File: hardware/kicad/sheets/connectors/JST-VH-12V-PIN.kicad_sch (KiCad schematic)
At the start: 5 parts, among them U58 VH3_96-2P_WZ

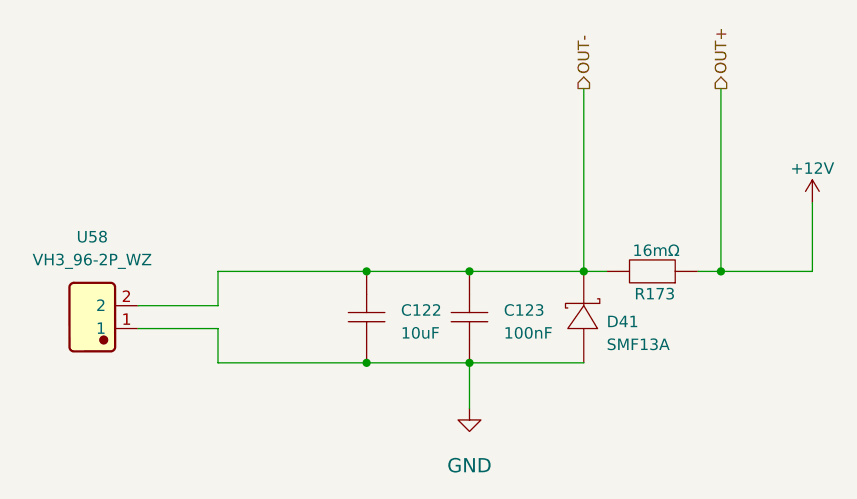
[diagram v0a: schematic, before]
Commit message: more sheet simplfiication and pre simpler 12v sym
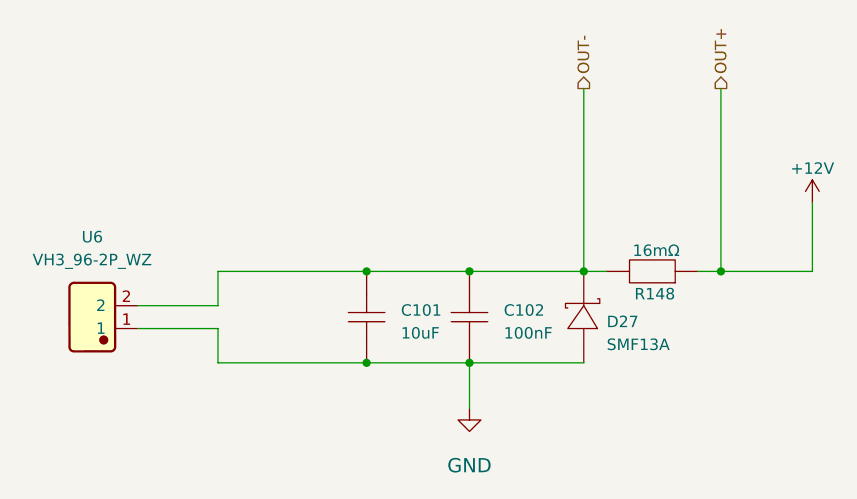
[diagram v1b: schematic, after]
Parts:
- renumbered C122 to C101, C123 to C102, D41 to D27, R173 to R148, U58 to U6

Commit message: resheeted bms and fixed links for the 12v buck
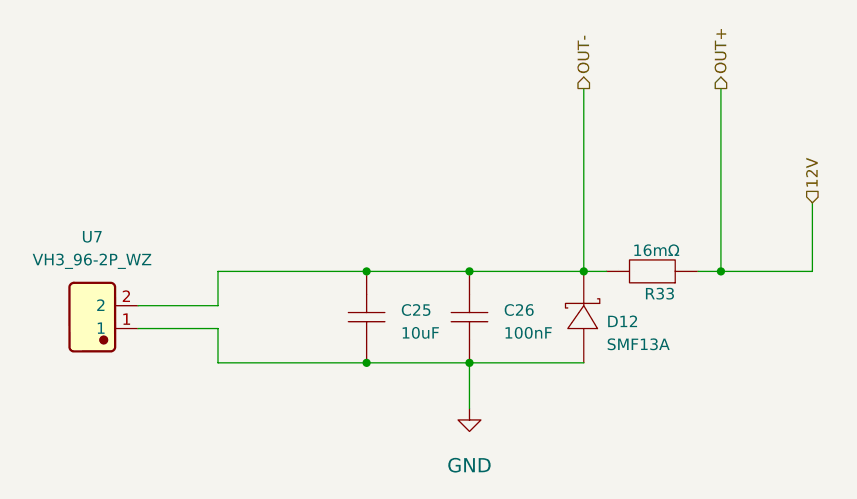
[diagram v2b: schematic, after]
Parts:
- renumbered C101 to C25, C102 to C26, D27 to D12, R148 to R33, U6 to U7
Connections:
- net +12V renamed 12V

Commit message: various improvements
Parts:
- renumbered C25 to C29, C26 to C30, D12 to D15, R33 to R35, U7 to U13
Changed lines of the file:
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@@
 		(on_board yes)
 		(dnp no)
-		(property "Reference" "U7"
+		(property "Reference" "U13"
 			(at 97.79 87.63 0)
 			(effects
@@
 			(project "svea_powerboard_rev3"
 				(path "/3f85abf4-0b95-4c4a-b7e9-06f59ca1ea3d/5c2e021f-c2d4-49e2-8c36-9a64f1f12001/03241f80-3125-4f5b-a1a0-add76ba31aaa"
-					(reference "U7")
-					(unit 1)
-				)
-				(path "/3f85abf4-0b95-4c4a-b7e9-06f59ca1ea3d/5c2e021f-c2d4-49e2-8c36-9a64f1f12001/b3c2b899-37d0-4be6-83c2-2e989d7fd2d2"
-					(reference "U8")
-					(unit 1)
-				)
-				(path "/3f85abf4-0b95-4c4a-b7e9-06f59ca1ea3d/5c2e021f-c2d4-49e2-8c36-9a64f1f12001/edc91f8c-d810-4cb3-9371-ed9a44c3aaeb"
-					(reference "U9")
+					(reference "U13")
+					(unit 1)
+				)
+				(path "/3f85abf4-0b95-4c4a-b7e9-06f59ca1ea3d/5c2e021f-c2d4-49e2-8c36-9a64f1f12001/782118f9-6c0b-4f5a-9c3b-1e5b8fc1f0ac"
+					(reference "U14")
+					(unit 1)
+				)
+				(path "/3f85abf4-0b95-4c4a-b7e9-06f59ca1ea3d/5c2e021f-c2d4-49e2-8c36-9a64f1f12001/beb9ceef-df3a-4e22-8974-012ce1407a41"
+					(reference "U15")
 					(unit 1)
 				)
@@
 		(on_board yes)
 		(dnp no)
-		(property "Reference" "D12"
+		(property "Reference" "D15"
 			(at 154.94 97.79 90)
 			(effects
@@
 			(project "svea_powerboard_rev3"
 				(path "/3f85abf4-0b95-4c4a-b7e9-06f59ca1ea3d/5c2e021f-c2d4-49e2-8c36-9a64f1f12001/03241f80-3125-4f5b-a1a0-add76ba31aaa"
-					(reference "D12")
-					(unit 1)
-				)
-				(path "/3f85abf4-0b95-4c4a-b7e9-06f59ca1ea3d/5c2e021f-c2d4-49e2-8c36-9a64f1f12001/b3c2b899-37d0-4be6-83c2-2e989d7fd2d2"
-					(reference "D13")
-					(unit 1)
-				)
-				(path "/3f85abf4-0b95-4c4a-b7e9-06f59ca1ea3d/5c2e021f-c2d4-49e2-8c36-9a64f1f12001/edc91f8c-d810-4cb3-9371-ed9a44c3aaeb"
-					(reference "D14")
+					(reference "D15")
+					(unit 1)
+				)
+				(path "/3f85abf4-0b95-4c4a-b7e9-06f59ca1ea3d/5c2e021f-c2d4-49e2-8c36-9a64f1f12001/782118f9-6c0b-4f5a-9c3b-1e5b8fc1f0ac"
+					(reference "D16")
+					(unit 1)
+				)
+				(path "/3f85abf4-0b95-4c4a-b7e9-06f59ca1ea3d/5c2e021f-c2d4-49e2-8c36-9a64f1f12001/beb9ceef-df3a-4e22-8974-012ce1407a41"
+					(reference "D17")
 					(unit 1)
 				)
@@
 		(on_board yes)
 		(dnp no)
-		(property "Reference" "C26"
+		(property "Reference" "C30"
 			(at 143.51 96.52 90)
 			(effects
@@
 			(project "svea_powerboard_rev3"
 				(path "/3f85abf4-0b95-4c4a-b7e9-06f59ca1ea3d/5c2e021f-c2d4-49e2-8c36-9a64f1f12001/03241f80-3125-4f5b-a1a0-add76ba31aaa"
-					(reference "C26")
-					(unit 1)
-				)
-				(path "/3f85abf4-0b95-4c4a-b7e9-06f59ca1ea3d/5c2e021f-c2d4-49e2-8c36-9a64f1f12001/b3c2b899-37d0-4be6-83c2-2e989d7fd2d2"
-					(reference "C28")
-					(unit 1)
-				)
-				(path "/3f85abf4-0b95-4c4a-b7e9-06f59ca1ea3d/5c2e021f-c2d4-49e2-8c36-9a64f1f12001/edc91f8c-d810-4cb3-9371-ed9a44c3aaeb"
 					(reference "C30")
+					(unit 1)
+				)
+				(path "/3f85abf4-0b95-4c4a-b7e9-06f59ca1ea3d/5c2e021f-c2d4-49e2-8c36-9a64f1f12001/782118f9-6c0b-4f5a-9c3b-1e5b8fc1f0ac"
+					(reference "C32")
+					(unit 1)
+				)
+				(path "/3f85abf4-0b95-4c4a-b7e9-06f59ca1ea3d/5c2e021f-c2d4-49e2-8c36-9a64f1f12001/beb9ceef-df3a-4e22-8974-012ce1407a41"
+					(reference "C34")
 					(unit 1)
 				)
@@
 		(on_board yes)
 		(dnp no)
-		(property "Reference" "#PWR035"
+		(property "Reference" "#PWR053"
 			(at 139.7 106.68 0)
 			(effects
@@
 			(project "svea_powerboard_rev3"
 				(path "/3f85abf4-0b95-4c4a-b7e9-06f59ca1ea3d/5c2e021f-c2d4-49e2-8c36-9a64f1f12001/03241f80-3125-4f5b-a1a0-add76ba31aaa"
-					(reference "#PWR035")
-					(unit 1)
-				)
-				(path "/3f85abf4-0b95-4c4a-b7e9-06f59ca1ea3d/5c2e021f-c2d4-49e2-8c36-9a64f1f12001/b3c2b899-37d0-4be6-83c2-2e989d7fd2d2"
-					(reference "#PWR036")
-					(unit 1)
-				)
-				(path "/3f85abf4-0b95-4c4a-b7e9-06f59ca1ea3d/5c2e021f-c2d4-49e2-8c36-9a64f1f12001/edc91f8c-d810-4cb3-9371-ed9a44c3aaeb"
-					(reference "#PWR037")
+					(reference "#PWR053")
+					(unit 1)
+				)
+				(path "/3f85abf4-0b95-4c4a-b7e9-06f59ca1ea3d/5c2e021f-c2d4-49e2-8c36-9a64f1f12001/782118f9-6c0b-4f5a-9c3b-1e5b8fc1f0ac"
+					(reference "#PWR054")
+					(unit 1)
+				)
+				(path "/3f85abf4-0b95-4c4a-b7e9-06f59ca1ea3d/5c2e021f-c2d4-49e2-8c36-9a64f1f12001/beb9ceef-df3a-4e22-8974-012ce1407a41"
+					(reference "#PWR055")
 					(unit 1)
 				)
@@
 		(on_board yes)
 		(dnp no)
-		(property "Reference" "C25"
+		(property "Reference" "C29"
 			(at 132.08 96.52 90)
 			(effects
@@
 			(project "svea_powerboard_rev3"
 				(path "/3f85abf4-0b95-4c4a-b7e9-06f59ca1ea3d/5c2e021f-c2d4-49e2-8c36-9a64f1f12001/03241f80-3125-4f5b-a1a0-add76ba31aaa"
-					(reference "C25")
-					(unit 1)
-				)
-				(path "/3f85abf4-0b95-4c4a-b7e9-06f59ca1ea3d/5c2e021f-c2d4-49e2-8c36-9a64f1f12001/b3c2b899-37d0-4be6-83c2-2e989d7fd2d2"
-					(reference "C27")
-					(unit 1)
-				)
-				(path "/3f85abf4-0b95-4c4a-b7e9-06f59ca1ea3d/5c2e021f-c2d4-49e2-8c36-9a64f1f12001/edc91f8c-d810-4cb3-9371-ed9a44c3aaeb"
 					(reference "C29")
+					(unit 1)
+				)
+				(path "/3f85abf4-0b95-4c4a-b7e9-06f59ca1ea3d/5c2e021f-c2d4-49e2-8c36-9a64f1f12001/782118f9-6c0b-4f5a-9c3b-1e5b8fc1f0ac"
+					(reference "C31")
+					(unit 1)
+				)
+				(path "/3f85abf4-0b95-4c4a-b7e9-06f59ca1ea3d/5c2e021f-c2d4-49e2-8c36-9a64f1f12001/beb9ceef-df3a-4e22-8974-012ce1407a41"
+					(reference "C33")
 					(unit 1)
 				)
@@
 		(on_board yes)
 		(dnp no)
-		(property "Reference" "R33"
+		(property "Reference" "R35"
 			(at 162.56 93.218 0)
 			(effects
@@
 			(project "svea_powerboard_rev3"
 				(path "/3f85abf4-0b95-4c4a-b7e9-06f59ca1ea3d/5c2e021f-c2d4-49e2-8c36-9a64f1f12001/03241f80-3125-4f5b-a1a0-add76ba31aaa"
-					(reference "R33")
-					(unit 1)
-				)
-				(path "/3f85abf4-0b95-4c4a-b7e9-06f59ca1ea3d/5c2e021f-c2d4-49e2-8c36-9a64f1f12001/b3c2b899-37d0-4be6-83c2-2e989d7fd2d2"
-					(reference "R34")
-					(unit 1)
-				)
-				(path "/3f85abf4-0b95-4c4a-b7e9-06f59ca1ea3d/5c2e021f-c2d4-49e2-8c36-9a64f1f12001/edc91f8c-d810-4cb3-9371-ed9a44c3aaeb"
 					(reference "R35")
 					(unit 1)
 				)
+				(path "/3f85abf4-0b95-4c4a-b7e9-06f59ca1ea3d/5c2e021f-c2d4-49e2-8c36-9a64f1f12001/782118f9-6c0b-4f5a-9c3b-1e5b8fc1f0ac"
+					(reference "R36")
+					(unit 1)
+				)
+				(path "/3f85abf4-0b95-4c4a-b7e9-06f59ca1ea3d/5c2e021f-c2d4-49e2-8c36-9a64f1f12001/beb9ceef-df3a-4e22-8974-012ce1407a41"
+					(reference "R37")
+					(unit 1)
+				)

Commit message: various improvements
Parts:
- renumbered C29 to C36, C30 to C37, D15 to D18, R35 to R44
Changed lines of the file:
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@@
 		(on_board yes)
 		(dnp no)
-		(property "Reference" "D15"
+		(property "Reference" "D18"
 			(at 154.94 97.79 90)
 			(effects
@@
 			(project "svea_powerboard_rev3"
 				(path "/3f85abf4-0b95-4c4a-b7e9-06f59ca1ea3d/5c2e021f-c2d4-49e2-8c36-9a64f1f12001/03241f80-3125-4f5b-a1a0-add76ba31aaa"
-					(reference "D15")
+					(reference "D18")
 					(unit 1)
 				)
 				(path "/3f85abf4-0b95-4c4a-b7e9-06f59ca1ea3d/5c2e021f-c2d4-49e2-8c36-9a64f1f12001/782118f9-6c0b-4f5a-9c3b-1e5b8fc1f0ac"
-					(reference "D16")
+					(reference "D19")
 					(unit 1)
 				)
 				(path "/3f85abf4-0b95-4c4a-b7e9-06f59ca1ea3d/5c2e021f-c2d4-49e2-8c36-9a64f1f12001/beb9ceef-df3a-4e22-8974-012ce1407a41"
-					(reference "D17")
+					(reference "D20")
 					(unit 1)
 				)
@@
 		(on_board yes)
 		(dnp no)
-		(property "Reference" "C30"
+		(property "Reference" "C37"
 			(at 143.51 96.52 90)
 			(effects
@@
 			(project "svea_powerboard_rev3"
 				(path "/3f85abf4-0b95-4c4a-b7e9-06f59ca1ea3d/5c2e021f-c2d4-49e2-8c36-9a64f1f12001/03241f80-3125-4f5b-a1a0-add76ba31aaa"
-					(reference "C30")
+					(reference "C37")
 					(unit 1)
 				)
 				(path "/3f85abf4-0b95-4c4a-b7e9-06f59ca1ea3d/5c2e021f-c2d4-49e2-8c36-9a64f1f12001/782118f9-6c0b-4f5a-9c3b-1e5b8fc1f0ac"
-					(reference "C32")
+					(reference "C39")
 					(unit 1)
 				)
 				(path "/3f85abf4-0b95-4c4a-b7e9-06f59ca1ea3d/5c2e021f-c2d4-49e2-8c36-9a64f1f12001/beb9ceef-df3a-4e22-8974-012ce1407a41"
-					(reference "C34")
+					(reference "C41")
 					(unit 1)
 				)
@@
 		(on_board yes)
 		(dnp no)
-		(property "Reference" "#PWR053"
+		(property "Reference" "#PWR061"
 			(at 139.7 106.68 0)
 			(effects
@@
 			(project "svea_powerboard_rev3"
 				(path "/3f85abf4-0b95-4c4a-b7e9-06f59ca1ea3d/5c2e021f-c2d4-49e2-8c36-9a64f1f12001/03241f80-3125-4f5b-a1a0-add76ba31aaa"
-					(reference "#PWR053")
+					(reference "#PWR061")
 					(unit 1)
 				)
 				(path "/3f85abf4-0b95-4c4a-b7e9-06f59ca1ea3d/5c2e021f-c2d4-49e2-8c36-9a64f1f12001/782118f9-6c0b-4f5a-9c3b-1e5b8fc1f0ac"
-					(reference "#PWR054")
+					(reference "#PWR062")
 					(unit 1)
 				)
 				(path "/3f85abf4-0b95-4c4a-b7e9-06f59ca1ea3d/5c2e021f-c2d4-49e2-8c36-9a64f1f12001/beb9ceef-df3a-4e22-8974-012ce1407a41"
-					(reference "#PWR055")
+					(reference "#PWR063")
 					(unit 1)
 				)
@@
 		(on_board yes)
 		(dnp no)
-		(property "Reference" "C29"
+		(property "Reference" "C36"
 			(at 132.08 96.52 90)
 			(effects
@@
 			(project "svea_powerboard_rev3"
 				(path "/3f85abf4-0b95-4c4a-b7e9-06f59ca1ea3d/5c2e021f-c2d4-49e2-8c36-9a64f1f12001/03241f80-3125-4f5b-a1a0-add76ba31aaa"
-					(reference "C29")
+					(reference "C36")
 					(unit 1)
 				)
 				(path "/3f85abf4-0b95-4c4a-b7e9-06f59ca1ea3d/5c2e021f-c2d4-49e2-8c36-9a64f1f12001/782118f9-6c0b-4f5a-9c3b-1e5b8fc1f0ac"
-					(reference "C31")
+					(reference "C38")
 					(unit 1)
 				)
 				(path "/3f85abf4-0b95-4c4a-b7e9-06f59ca1ea3d/5c2e021f-c2d4-49e2-8c36-9a64f1f12001/beb9ceef-df3a-4e22-8974-012ce1407a41"
-					(reference "C33")
+					(reference "C40")
 					(unit 1)
 				)
@@
 		(on_board yes)
 		(dnp no)
-		(property "Reference" "R35"
+		(property "Reference" "R44"
 			(at 162.56 93.218 0)
 			(effects
@@
 			(project "svea_powerboard_rev3"
 				(path "/3f85abf4-0b95-4c4a-b7e9-06f59ca1ea3d/5c2e021f-c2d4-49e2-8c36-9a64f1f12001/03241f80-3125-4f5b-a1a0-add76ba31aaa"
-					(reference "R35")
+					(reference "R44")
 					(unit 1)
 				)
 				(path "/3f85abf4-0b95-4c4a-b7e9-06f59ca1ea3d/5c2e021f-c2d4-49e2-8c36-9a64f1f12001/782118f9-6c0b-4f5a-9c3b-1e5b8fc1f0ac"
-					(reference "R36")
+					(reference "R45")
 					(unit 1)
 				)
 				(path "/3f85abf4-0b95-4c4a-b7e9-06f59ca1ea3d/5c2e021f-c2d4-49e2-8c36-9a64f1f12001/beb9ceef-df3a-4e22-8974-012ce1407a41"
-					(reference "R37")
-					(unit 1)
-				)
+					(reference "R46")
+					(unit 1)
+				)

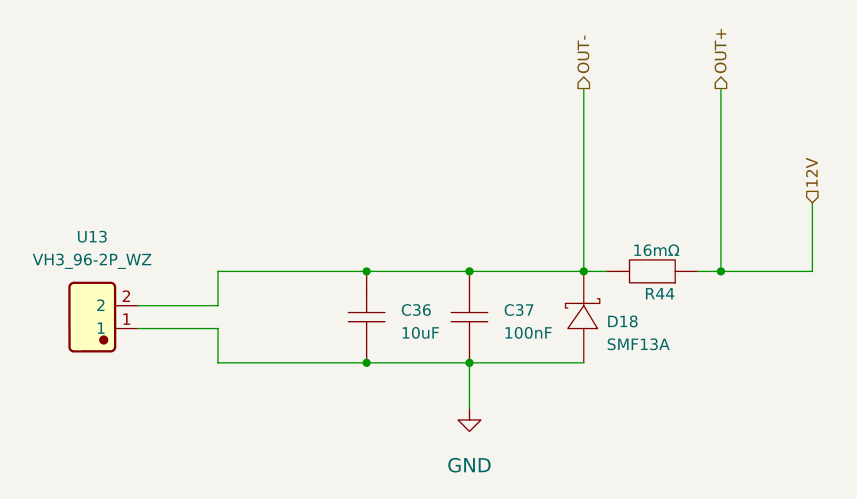
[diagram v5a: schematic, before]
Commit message: current sensing on the servos and cleaning up empty sheets
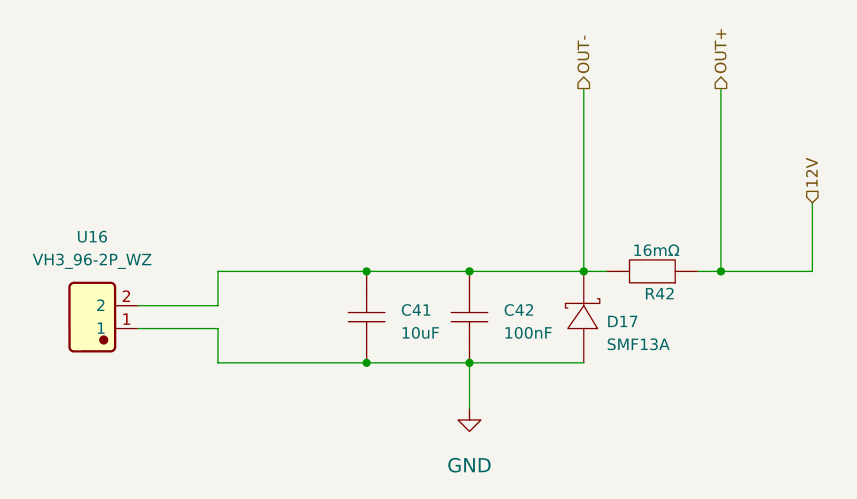
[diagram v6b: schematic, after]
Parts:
- renumbered C36 to C41, C37 to C42, D18 to D17, R44 to R42, U13 to U16
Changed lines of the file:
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@@
 		(on_board yes)
 		(dnp no)
-		(property "Reference" "U13"
+		(property "Reference" "U16"
 			(at 97.79 87.63 0)
 			(effects
@@
 			(project "svea_powerboard_rev3"
 				(path "/3f85abf4-0b95-4c4a-b7e9-06f59ca1ea3d/5c2e021f-c2d4-49e2-8c36-9a64f1f12001/03241f80-3125-4f5b-a1a0-add76ba31aaa"
-					(reference "U13")
+					(reference "U16")
 					(unit 1)
 				)
 				(path "/3f85abf4-0b95-4c4a-b7e9-06f59ca1ea3d/5c2e021f-c2d4-49e2-8c36-9a64f1f12001/782118f9-6c0b-4f5a-9c3b-1e5b8fc1f0ac"
-					(reference "U14")
+					(reference "U17")
 					(unit 1)
 				)
 				(path "/3f85abf4-0b95-4c4a-b7e9-06f59ca1ea3d/5c2e021f-c2d4-49e2-8c36-9a64f1f12001/beb9ceef-df3a-4e22-8974-012ce1407a41"
-					(reference "U15")
+					(reference "U18")
 					(unit 1)
 				)
@@
 		(on_board yes)
 		(dnp no)
-		(property "Reference" "D18"
+		(property "Reference" "D17"
 			(at 154.94 97.79 90)
 			(effects
@@
 			(project "svea_powerboard_rev3"
 				(path "/3f85abf4-0b95-4c4a-b7e9-06f59ca1ea3d/5c2e021f-c2d4-49e2-8c36-9a64f1f12001/03241f80-3125-4f5b-a1a0-add76ba31aaa"
+					(reference "D17")
+					(unit 1)
+				)
+				(path "/3f85abf4-0b95-4c4a-b7e9-06f59ca1ea3d/5c2e021f-c2d4-49e2-8c36-9a64f1f12001/782118f9-6c0b-4f5a-9c3b-1e5b8fc1f0ac"
 					(reference "D18")
 					(unit 1)
 				)
-				(path "/3f85abf4-0b95-4c4a-b7e9-06f59ca1ea3d/5c2e021f-c2d4-49e2-8c36-9a64f1f12001/782118f9-6c0b-4f5a-9c3b-1e5b8fc1f0ac"
+				(path "/3f85abf4-0b95-4c4a-b7e9-06f59ca1ea3d/5c2e021f-c2d4-49e2-8c36-9a64f1f12001/beb9ceef-df3a-4e22-8974-012ce1407a41"
 					(reference "D19")
-					(unit 1)
-				)
-				(path "/3f85abf4-0b95-4c4a-b7e9-06f59ca1ea3d/5c2e021f-c2d4-49e2-8c36-9a64f1f12001/beb9ceef-df3a-4e22-8974-012ce1407a41"
-					(reference "D20")
 					(unit 1)
 				)
@@
 		(on_board yes)
 		(dnp no)
-		(property "Reference" "C37"
+		(property "Reference" "C42"
 			(at 143.51 96.52 90)
 			(effects
@@
 			(project "svea_powerboard_rev3"
 				(path "/3f85abf4-0b95-4c4a-b7e9-06f59ca1ea3d/5c2e021f-c2d4-49e2-8c36-9a64f1f12001/03241f80-3125-4f5b-a1a0-add76ba31aaa"
-					(reference "C37")
+					(reference "C42")
 					(unit 1)
 				)
 				(path "/3f85abf4-0b95-4c4a-b7e9-06f59ca1ea3d/5c2e021f-c2d4-49e2-8c36-9a64f1f12001/782118f9-6c0b-4f5a-9c3b-1e5b8fc1f0ac"
-					(reference "C39")
+					(reference "C44")
 					(unit 1)
 				)
 				(path "/3f85abf4-0b95-4c4a-b7e9-06f59ca1ea3d/5c2e021f-c2d4-49e2-8c36-9a64f1f12001/beb9ceef-df3a-4e22-8974-012ce1407a41"
-					(reference "C41")
+					(reference "C46")
 					(unit 1)
 				)
@@
 		(on_board yes)
 		(dnp no)
-		(property "Reference" "#PWR061"
+		(property "Reference" "#PWR062"
 			(at 139.7 106.68 0)
 			(effects
@@
 			(project "svea_powerboard_rev3"
 				(path "/3f85abf4-0b95-4c4a-b7e9-06f59ca1ea3d/5c2e021f-c2d4-49e2-8c36-9a64f1f12001/03241f80-3125-4f5b-a1a0-add76ba31aaa"
-					(reference "#PWR061")
+					(reference "#PWR062")
 					(unit 1)
 				)
 				(path "/3f85abf4-0b95-4c4a-b7e9-06f59ca1ea3d/5c2e021f-c2d4-49e2-8c36-9a64f1f12001/782118f9-6c0b-4f5a-9c3b-1e5b8fc1f0ac"
-					(reference "#PWR062")
+					(reference "#PWR063")
 					(unit 1)
 				)
 				(path "/3f85abf4-0b95-4c4a-b7e9-06f59ca1ea3d/5c2e021f-c2d4-49e2-8c36-9a64f1f12001/beb9ceef-df3a-4e22-8974-012ce1407a41"
-					(reference "#PWR063")
+					(reference "#PWR064")
 					(unit 1)
 				)
@@
 		(on_board yes)
 		(dnp no)
-		(property "Reference" "C36"
+		(property "Reference" "C41"
 			(at 132.08 96.52 90)
 			(effects
@@
 			(project "svea_powerboard_rev3"
 				(path "/3f85abf4-0b95-4c4a-b7e9-06f59ca1ea3d/5c2e021f-c2d4-49e2-8c36-9a64f1f12001/03241f80-3125-4f5b-a1a0-add76ba31aaa"
-					(reference "C36")
+					(reference "C41")
 					(unit 1)
 				)
 				(path "/3f85abf4-0b95-4c4a-b7e9-06f59ca1ea3d/5c2e021f-c2d4-49e2-8c36-9a64f1f12001/782118f9-6c0b-4f5a-9c3b-1e5b8fc1f0ac"
-					(reference "C38")
+					(reference "C43")
 					(unit 1)
 				)
 				(path "/3f85abf4-0b95-4c4a-b7e9-06f59ca1ea3d/5c2e021f-c2d4-49e2-8c36-9a64f1f12001/beb9ceef-df3a-4e22-8974-012ce1407a41"
-					(reference "C40")
+					(reference "C45")
 					(unit 1)
 				)
@@
 		(on_board yes)
 		(dnp no)
-		(property "Reference" "R44"
+		(property "Reference" "R42"
 			(at 162.56 93.218 0)
 			(effects
@@
 			(project "svea_powerboard_rev3"
 				(path "/3f85abf4-0b95-4c4a-b7e9-06f59ca1ea3d/5c2e021f-c2d4-49e2-8c36-9a64f1f12001/03241f80-3125-4f5b-a1a0-add76ba31aaa"
+					(reference "R42")
+					(unit 1)
+				)
+				(path "/3f85abf4-0b95-4c4a-b7e9-06f59ca1ea3d/5c2e021f-c2d4-49e2-8c36-9a64f1f12001/782118f9-6c0b-4f5a-9c3b-1e5b8fc1f0ac"
+					(reference "R43")
+					(unit 1)
+				)
+				(path "/3f85abf4-0b95-4c4a-b7e9-06f59ca1ea3d/5c2e021f-c2d4-49e2-8c36-9a64f1f12001/beb9ceef-df3a-4e22-8974-012ce1407a41"
 					(reference "R44")
 					(unit 1)
 				)
-				(path "/3f85abf4-0b95-4c4a-b7e9-06f59ca1ea3d/5c2e021f-c2d4-49e2-8c36-9a64f1f12001/782118f9-6c0b-4f5a-9c3b-1e5b8fc1f0ac"
-					(reference "R45")
-					(unit 1)
-				)
-				(path "/3f85abf4-0b95-4c4a-b7e9-06f59ca1ea3d/5c2e021f-c2d4-49e2-8c36-9a64f1f12001/beb9ceef-df3a-4e22-8974-012ce1407a41"
-					(reference "R46")
-					(unit 1)
-				)
